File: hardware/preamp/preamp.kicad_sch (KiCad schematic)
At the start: 31 parts, among them J1 I/O, J2 Conn 1, J3 Conn 2, Q1 2SC3324, Q2 2SC3324, U1 TLV170DBV

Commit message: WIP
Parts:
- removed D1: CUS551V30,H3F, Diode_SMD:D_SOD-323, symbol Device:D_Schottky_ALT
- removed H1, H2, H3, H4: MountingHole, cycfi_library:mounting_hole_st1.9, symbol Mechanical:MountingHole
- removed J1: I/O, cycfi_library:pin_header_2x5p_2.54mm_smd_horizontal, symbol Connector_Generic:Conn_02x05_Counter_Clockwise
- removed J2: Conn 1, cycfi_library:pin_socket_2x3p_1.00mm_smd_vertical, symbol Connector_Generic:Conn_02x03_Counter_Clockwise
- removed J3: Conn 2, cycfi_library:pin_socket_2x3p_1.00mm_smd_vertical, symbol Connector_Generic:Conn_02x03_Counter_Clockwise
- removed JP1: Coil Shunt, Jumper:SolderJumper-2_P1.3mm_Open_TrianglePad1.0x1.5mm, symbol Jumper:Jumper_2_Open
- removed Q1, Q2: 2SC3324, Package_TO_SOT_SMD:SOT-23, symbol cycfi_library:npn_bec
- removed R1, R8: 100k, Resistor_SMD:R_0402_1005Metric, symbol Device:R
- removed R2, R9: 51k, Resistor_SMD:R_0402_1005Metric, symbol Device:R
- removed R3, R6: 39k, Resistor_SMD:R_0402_1005Metric, symbol Device:R
- removed R4, R7: 1k, Resistor_SMD:R_0402_1005Metric, symbol Device:R
- removed R5: 10k, Resistor_SMD:R_0402_1005Metric, symbol Device:R
- added C1, C2: 10uF, Capacitor_SMD:C_0603_1608Metric, symbol Device:C
- added J1, J2: conn_1x3, cycfi_library:pin_header_1x3p_2.54mm_smd_horizontal, symbol cycfi_library:conn_1x3
- added Q1: q_pmos_gsd, Package_TO_SOT_SMD:TSOT-23, symbol cycfi_library:q_pmos_gsd
- R1: renamed from R10; value 39k -> 10k
- R2: renamed from R11; value 39k -> 10k
- R3: renamed from R12; value 200k -> 300k
- R4: renamed from R13; value 200k -> 300k
- R5: renamed from R14; value 100k -> 150k
- R6: renamed from R15; value 10k -> 47k
- U1: value TLV170DBV -> TLV170IDBV; symbol cycfi_library:TLV170DBV -> cycfi_library:opamp_dbv
- renumbered C1 to C4, C2 to C5, R16 to R7
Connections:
- net V+ is gone; now on net vcc: C4.1, C5.1, R3.1, U1.5 (V+)
- net mix is gone; now on net out: R7.1
- net GND: now also J1.2 (P2), J2.2 (P2), Q1.1 (G)
- net in-: now also C2.2, J1.3 (P3)
- net out: now also J2.1 (P1); no longer C3.1, R6.1, R7.2
- net vcc: now also Q1.2 (S)
- net opamp_out: now reaches C3.2, R5.2, U1.1
- net op_amp+: now reaches R1.1, R3.2, R4.1, U1.3 (+)
- net op_amp-: now reaches R2.2, R5.1, U1.4 (-)
- net at R1.2: now also C1.1
- net at R2.1: now also C2.1
- new net: C3.1, R6.1, R7.2
- new net in+: C1.2, J1.1 (P1)
- new net v+: J2.3 (P3), Q1.3 (D)
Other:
- note added: "Balanced Preamplifier"
- note added: "Input"
- note added: "Output"
- note removed: "1, 2: External coil shunt 3, 4, 5: External coil"
- note removed: "6, 7, 8: Main output and power 9, 10: Mixing resistor shunt"
- note removed: "Main Coil"
- note removed: "Redundant connections to the coil via two small 1mm 2x3 connectors for improved reliability."
- moved on the sheet: C3, C4, C5, R1, R2, R3, R4, R5, R6, R7

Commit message: OK. Looks good.
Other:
- note added: "2.0"
- note added: "March 10, 2022"
- note removed: "1.0"
- note removed: "June 17, 2021"
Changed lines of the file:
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@@
     (effects (font (size 1.27 1.27)) (justify left bottom))
   )
-  (text "1.0" (at 269.24 194.31 0)
+  (text "2.0" (at 269.24 194.31 0)
     (effects (font (size 1.27 1.27)) (justify left bottom))
   )
-  (text "June 17, 2021" (at 207.01 194.31 0)
+  (text "March 10, 2022" (at 207.01 194.31 0)
     (effects (font (size 1.27 1.27)) (justify left bottom))
   )

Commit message: Back to floating differential
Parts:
- removed C2: 10uF, Capacitor_SMD:C_0603_1608Metric, symbol Device:C
- C1: value 10uF -> 100pF; footprint Capacitor_SMD:C_0603_1608Metric -> Capacitor_SMD:C_0402_1005Metric
- C2: renamed from C3; footprint Capacitor_SMD:C_0603_1608Metric -> Capacitor_SMD:C_0805_2012Metric
- C3: renamed from C4; footprint Capacitor_SMD:C_0603_1608Metric -> Capacitor_SMD:C_0805_2012Metric
- Q1: value q_pmos_gsd -> LBSS84LT1G
- renumbered C5 to C4
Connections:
- net in+: now also C1.1, R1.2; no longer C1.2
- net in-: now also C1.2, R2.1
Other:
- moved on the sheet: R1, R2

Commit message: Finalize schematics
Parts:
- C1: LCSC (none) -> C1546
- C2: LCSC (none) -> C15850
- C3: LCSC (none) -> C1779
- C4: value 0.1uF -> 100nF; LCSC (none) -> C307331
- Q1: JLCPCB_CORRECTION (none) -> 0;0;0; LCSC (none) -> C8492
- R1, R2: value 10k -> 15k; LCSC (none) -> C25756
- R3, R4: value 300k -> 150k; LCSC (none) -> C25755
- R5: value 150k -> 75k; LCSC (none) -> C25798
- R6: LCSC (none) -> C25792
- R7: LCSC (none) -> C25900
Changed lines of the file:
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@@
     (in_bom yes) (on_board yes)
     (property "Reference" "R1" (id 0) (at 110.49 110.3122 90))
-    (property "Value" "10k" (id 1) (at 110.49 112.6236 90))
+    (property "Value" "15k" (id 1) (at 110.49 112.6236 90))
     (property "Footprint" "Resistor_SMD:R_0402_1005Metric" (id 2) (at 110.49 113.792 90)
       (effects (font (size 1.27 1.27)) hide)
@@
       (effects (font (size 1.27 1.27)) hide)
     )
+    (property "LCSC" "C25756" (id 4) (at 110.49 115.57 0)
+      (effects (font (size 1.27 1.27)) hide)
+    )
     (pin "1")
     (pin "2")
@@
     (in_bom yes) (on_board yes)
     (property "Reference" "R2" (id 0) (at 110.49 133.5278 90))
-    (property "Value" "10k" (id 1) (at 110.49 131.2164 90))
+    (property "Value" "15k" (id 1) (at 110.49 131.2164 90))
     (property "Footprint" "Resistor_SMD:R_0402_1005Metric" (id 2) (at 110.49 130.048 90)
       (effects (font (size 1.27 1.27)) hide)
@@
       (effects (font (size 1.27 1.27)) hide)
     )
+    (property "LCSC" "C25756" (id 4) (at 110.49 128.27 0)
+      (effects (font (size 1.27 1.27)) hide)
+    )
     (pin "1")
     (pin "2")
@@
     (in_bom yes) (on_board yes)
     (property "Reference" "R3" (id 0) (at 124.46 91.2622 90))
-    (property "Value" "300k" (id 1) (at 124.46 93.5736 90))
+    (property "Value" "150k" (id 1) (at 124.46 93.5736 90))
     (property "Footprint" "Resistor_SMD:R_0402_1005Metric" (id 2) (at 124.46 98.298 90)
       (effects (font (size 1.27 1.27)) hide)
@@
       (effects (font (size 1.27 1.27)) hide)
     )
+    (property "LCSC" "C25755" (id 4) (at 124.46 96.52 0)
+      (effects (font (size 1.27 1.27)) hide)
+    )
     (pin "1")
     (pin "2")
@@
     (in_bom yes) (on_board yes)
     (property "Reference" "R4" (id 0) (at 139.7 91.2622 90))
-    (property "Value" "300k" (id 1) (at 139.7 93.5736 90))
+    (property "Value" "150k" (id 1) (at 139.7 93.5736 90))
     (property "Footprint" "Resistor_SMD:R_0402_1005Metric" (id 2) (at 139.7 98.298 90)
       (effects (font (size 1.27 1.27)) hide)
@@
       (effects (font (size 1.27 1.27)) hide)
     )
+    (property "LCSC" "C25755" (id 4) (at 139.7 96.52 0)
+      (effects (font (size 1.27 1.27)) hide)
+    )
     (pin "1")
     (pin "2")
@@
     (in_bom yes) (on_board yes)
     (property "Reference" "R5" (id 0) (at 147.32 143.51 90))
-    (property "Value" "150k" (id 1) (at 147.32 146.05 90))
+    (property "Value" "75k" (id 1) (at 147.32 146.05 90))
     (property "Footprint" "Resistor_SMD:R_0402_1005Metric" (id 2) (at 147.32 142.748 90)
       (effects (font (size 1.27 1.27)) hide)
     )
     (property "Datasheet" "~" (id 3) (at 147.32 140.97 0)
+      (effects (font (size 1.27 1.27)) hide)
+    )
+    (property "LCSC" "C25798" (id 4) (at 147.32 140.97 0)
       (effects (font (size 1.27 1.27)) hide)
     )
@@
       (effects (font (size 1.27 1.27)) hide)
     )
+    (property "LCSC" "C1779" (id 4) (at 186.69 55.88 0)
+      (effects (font (size 1.27 1.27)) hide)
+    )
     (pin "1")
     (pin "2")
@@
       (effects (font (size 1.27 1.27)) (justify left))
     )
-    (property "Value" "0.1uF" (id 1) (at 201.041 57.023 0)
+    (property "Value" "100nF" (id 1) (at 201.041 57.023 0)
       (effects (font (size 1.27 1.27)) (justify left))
     )
@@
     )
     (property "Datasheet" "~" (id 3) (at 198.12 55.88 0)
+      (effects (font (size 1.27 1.27)) hide)
+    )
+    (property "LCSC" "C307331" (id 4) (at 198.12 55.88 0)
       (effects (font (size 1.27 1.27)) hide)
     )
@@
       (effects (font (size 1.27 1.27)) hide)
     )
+    (property "LCSC" "C15850" (id 4) (at 172.72 121.92 0)
+      (effects (font (size 1.27 1.27)) hide)
+    )
     (pin "1")
     (pin "2")
@@
     )
     (property "Datasheet" "~" (id 3) (at 182.88 132.08 0)
+      (effects (font (size 1.27 1.27)) hide)
+    )
+    (property "LCSC" "C25792" (id 4) (at 182.88 132.08 0)
       (effects (font (size 1.27 1.27)) hide)
     )
@@
       (effects (font (size 1.27 1.27)) hide)
     )
+    (property "LCSC" "C25900" (id 4) (at 193.04 121.92 0)
+      (effects (font (size 1.27 1.27)) hide)
+    )
     (pin "1")
     (pin "2")
@@
     )
     (property "Datasheet" "~" (id 3) (at 102.87 121.92 0)
+      (effects (font (size 1.27 1.27)) hide)
+    )
+    (property "LCSC" "C1546" (id 4) (at 102.87 121.92 0)
       (effects (font (size 1.27 1.27)) hide)
     )
@@
       (effects (font (size 1.27 1.27)) hide)
     )
+    (property "LCSC" "C8492" (id 4) (at 175.26 48.26 0)
+      (effects (font (size 1.27 1.27)) hide)
+    )
+    (property "JLCPCB_CORRECTION" "0;0;0" (id 5) (at 175.26 48.26 90)
+      (effects (font (size 1.27 1.27)) hide)
+    )
     (pin "1")
     (pin "2")
@@
     )
     (path "/00000000-0000-0000-0000-000060ccb141"
-      (reference "C4") (unit 1) (value "0.1uF") (footprint "Capacitor_SMD:C_0402_1005Metric")
+      (reference "C4") (unit 1) (value "100nF") (footprint "Capacitor_SMD:C_0402_1005Metric")
     )
     (path "/6724d18b-2934-4430-98a8-ebcd97522ce0"
@@
     )
     (path "/00000000-0000-0000-0000-000060ca74d0"
-      (reference "R1") (unit 1) (value "10k") (footprint "Resistor_SMD:R_0402_1005Metric")
+      (reference "R1") (unit 1) (value "15k") (footprint "Resistor_SMD:R_0402_1005Metric")
     )
     (path "/00000000-0000-0000-0000-000060ca8735"
-      (reference "R2") (unit 1) (value "10k") (footprint "Resistor_SMD:R_0402_1005Metric")
+      (reference "R2") (unit 1) (value "15k") (footprint "Resistor_SMD:R_0402_1005Metric")
     )
     (path "/00000000-0000-0000-0000-000060ca90d5"
-      (reference "R3") (unit 1) (value "300k") (footprint "Resistor_SMD:R_0402_1005Metric")
+      (reference "R3") (unit 1) (value "150k") (footprint "Resistor_SMD:R_0402_1005Metric")
     )
     (path "/00000000-0000-0000-0000-000060caa1e5"
-      (reference "R4") (unit 1) (value "300k") (footprint "Resistor_SMD:R_0402_1005Metric")
+      (reference "R4") (unit 1) (value "150k") (footprint "Resistor_SMD:R_0402_1005Metric")
     )
     (path "/00000000-0000-0000-0000-000060caa986"
-      (reference "R5") (unit 1) (value "150k") (footprint "Resistor_SMD:R_0402_1005Metric")
+      (reference "R5") (unit 1) (value "75k") (footprint "Resistor_SMD:R_0402_1005Metric")
     )
     (path "/00000000-0000-0000-0000-000060ce0f70"

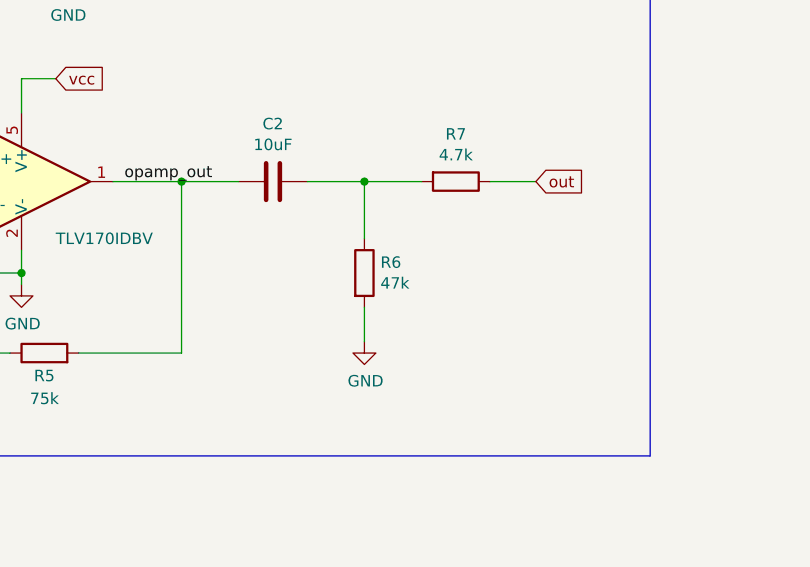
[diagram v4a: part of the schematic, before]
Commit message: Updated. Increased bleed resistor to 100k.
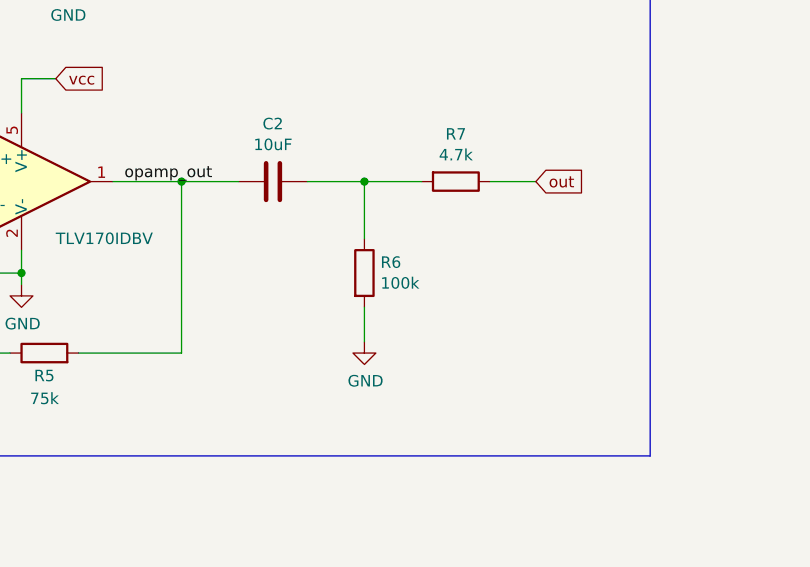
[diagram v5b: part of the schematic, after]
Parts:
- R6: value 47k -> 100k; LCSC C25792 -> C25741
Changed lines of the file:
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@@
       (effects (font (size 1.27 1.27)) (justify left))
     )
-    (property "Value" "47k" (id 1) (at 184.658 133.223 0)
+    (property "Value" "100k" (id 1) (at 184.658 133.223 0)
       (effects (font (size 1.27 1.27)) (justify left))
     )
@@
       (effects (font (size 1.27 1.27)) hide)
     )
-    (property "LCSC" "C25792" (id 4) (at 182.88 132.08 0)
+    (property "LCSC" "C25741" (id 4) (at 182.88 132.08 0)
       (effects (font (size 1.27 1.27)) hide)
     )
@@
     )
     (path "/00000000-0000-0000-0000-000060ce0f70"
-      (reference "R6") (unit 1) (value "47k") (footprint "Resistor_SMD:R_0402_1005Metric")
+      (reference "R6") (unit 1) (value "100k") (footprint "Resistor_SMD:R_0402_1005Metric")
     )
     (path "/00000000-0000-0000-0000-000060ce1d3d"

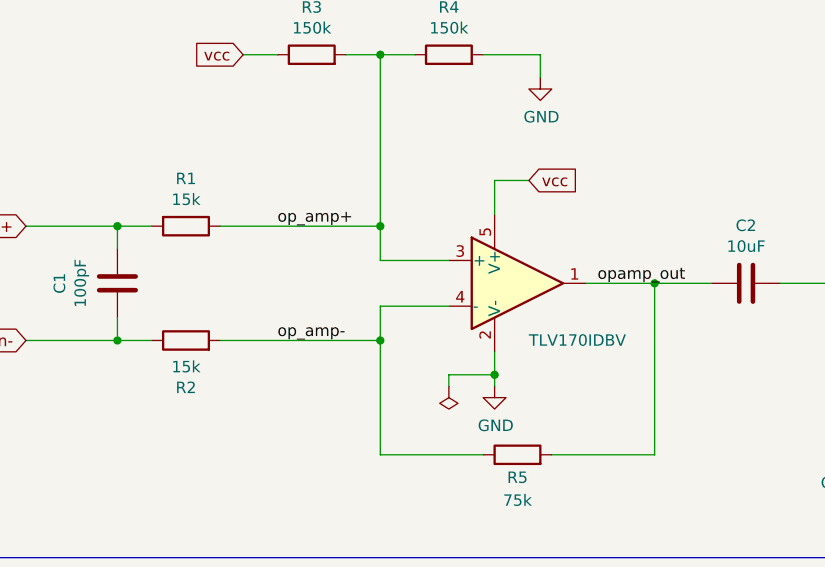
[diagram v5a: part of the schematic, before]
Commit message: V3.0 Increase gain to 10
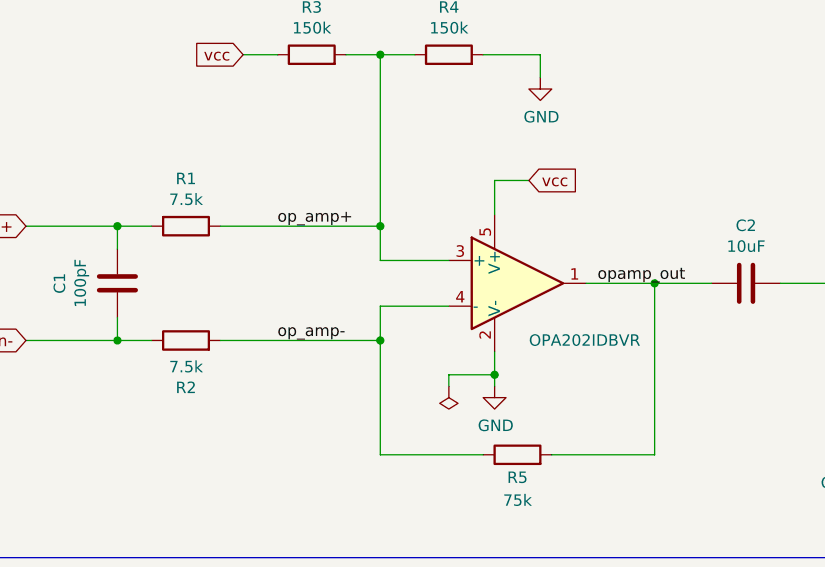
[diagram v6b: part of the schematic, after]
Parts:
- R1, R2: value 15k -> 7.5k; LCSC C25756 -> C25918
- U1: value TLV170IDBV -> OPA202IDBVR; LCSC (none) -> C1850244
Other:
- company: (none) -> Document No. 2024008
- title: (none) -> XR Spectra Preamp
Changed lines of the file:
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@@
 (kicad_sch (version 20211123) (generator eeschema)
   (paper "A4")
+  (title_block
+    (title "XR Spectra Preamp")
+    (date "2024-12-02")
+    (rev "3.0")
+    (company "Document No. 2024008")
+  )
   (junction (at 132.08 96.52) (diameter 0) (color 0 0 0 0)
   )
@@
       (effects (font (size 1.27 1.27)) (justify left) hide)
     )
-    (property "Value" "TLV170IDBV" (id 1) (at 148.59 128.27 0)
+    (property "Value" "OPA202IDBVR" (id 1) (at 148.59 128.27 0)
       (effects (font (size 1.27 1.27)) (justify left))
     )
@@
       (effects (font (size 1.27 1.27)) (justify left) hide)
     )
-    (property "Datasheet" "https://www.ti.com/lit/ds/symlink/tlv170.pdf" (id 3) (at 147.32 116.84 0)
+    (property "Datasheet" "https://www.ti.com/lit/gpn/OPA202" (id 3) (at 147.32 116.84 0)
+      (effects (font (size 1.27 1.27)) hide)
+    )
+    (property "LCSC" "C1850244" (id 4) (at 147.32 121.92 0)
       (effects (font (size 1.27 1.27)) hide)
     )
@@
     (in_bom yes) (on_board yes)
     (property "Reference" "R1" (id 0) (at 110.49 110.3122 90))
-    (property "Value" "15k" (id 1) (at 110.49 112.6236 90))
+    (property "Value" "7.5k" (id 1) (at 110.49 112.6236 90))
     (property "Footprint" "Resistor_SMD:R_0402_1005Metric" (id 2) (at 110.49 113.792 90)
       (effects (font (size 1.27 1.27)) hide)
@@
       (effects (font (size 1.27 1.27)) hide)
     )
-    (property "LCSC" "C25756" (id 4) (at 110.49 115.57 0)
+    (property "LCSC" "C25918" (id 4) (at 110.49 115.57 0)
       (effects (font (size 1.27 1.27)) hide)
     )
@@
     (in_bom yes) (on_board yes)
     (property "Reference" "R2" (id 0) (at 110.49 133.5278 90))
-    (property "Value" "15k" (id 1) (at 110.49 131.2164 90))
+    (property "Value" "7.5k" (id 1) (at 110.49 131.2164 90))
     (property "Footprint" "Resistor_SMD:R_0402_1005Metric" (id 2) (at 110.49 130.048 90)
       (effects (font (size 1.27 1.27)) hide)
@@
       (effects (font (size 1.27 1.27)) hide)
     )
-    (property "LCSC" "C25756" (id 4) (at 110.49 128.27 0)
+    (property "LCSC" "C25918" (id 4) (at 110.49 128.27 0)
       (effects (font (size 1.27 1.27)) hide)
     )
@@
     )
     (path "/00000000-0000-0000-0000-000060ca74d0"
-      (reference "R1") (unit 1) (value "15k") (footprint "Resistor_SMD:R_0402_1005Metric")
+      (reference "R1") (unit 1) (value "7.5k") (footprint "Resistor_SMD:R_0402_1005Metric")
     )
     (path "/00000000-0000-0000-0000-000060ca8735"
-      (reference "R2") (unit 1) (value "15k") (footprint "Resistor_SMD:R_0402_1005Metric")
+      (reference "R2") (unit 1) (value "7.5k") (footprint "Resistor_SMD:R_0402_1005Metric")
     )
     (path "/00000000-0000-0000-0000-000060ca90d5"
@@
     )
     (path "/00000000-0000-0000-0000-000060ca2d4c"
-      (reference "U1") (unit 1) (value "TLV170IDBV") (footprint "Package_TO_SOT_SMD:SOT-23-5")
-    )
-  )
+      (reference "U1") (unit 1) (value "OPA202IDBVR") (footprint "Package_TO_SOT_SMD:SOT-23-5")
+    )
+  )
